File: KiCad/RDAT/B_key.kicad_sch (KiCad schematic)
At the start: 0 parts

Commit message: Connected m.2 E Key
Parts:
- added C25: 22uF/6.3V, symbol Device:C_Small
- added C26: 10uF/6.3v, symbol Device:C_Small
- added C27: 0.1uF/16v, symbol Device:C_Small
- added C28, C29: 0.1uF/16V, symbol Device:C_Small
- added C30: 1uF/6.3v, symbol Device:C_Small
- added C31: 100fP/50V, symbol Device:C_Small
- added D110, D118: SD05_SOD323, Diode_SMD:D_SOD-323, symbol Diode:SD05_SOD323
- added D119, D120, D121, D122: ESD9B5.0ST5G, Diode_SMD:D_SOD-923, symbol Diode:ESD9B5.0ST5G
- added J3: Bus_M.2_Socket_B, symbol Connector:Bus_M.2_Socket_B
- added J4: SIM_Card, symbol Connector:SIM_Card
- added R28, R29: 10k, symbol Device:R_Small_US
- added R30, R78, R79, R83, R84: 0R, symbol Device:R_Small_US
- added R80, R81, R82: 15R, symbol Device:R_Small_US
- added TP13, TP14, TP15, TP16: TestPoint, symbol Connector:TestPoint
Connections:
- new net: J3.6 (~{FULL_CARD_POWER_OFF}), R29.2, R30.2, R78.1
- new net: J3.34 (UIM-DATA), R80.2
- new net: J3.68 (SUSCLK), TP16.1
- new net: J3.1 (CONFIG_3), TP14.1
- new net: J3.66 (SIM_DETECT), R79.1
- new net: J3.21 (CONFIG_0), TP15.1
- new net: J3.23 (GPIO_11), TP13.1
- new net: J3.30 (UIM-RESET), R82.2
- new net: J3.32 (UIM-CLK), R81.2
- new net: C29.2, J3.35 (PETn1/USB3.0-Tx-/SSIC-TxN)
- new net: C28.2, J3.37 (PETp1/USB3.0-Tx+/SSIC-TxP)
- new net: J3.67 (~{RESET}), R83.2, R84.2
- new net: J3.8 (~{W_DISABLE1}), R28.2
- new net: C31.2, J4.6 (VPP)
- new net +3V3: C25.1, C26.1, C27.1, J3.2 (3.3V), J3.4 (3.3V), J3.70 (3.3V), J3.72 (3.3V), J3.74 (3.3V), R28.1, R29.1
- new net GND: C25.2, C26.2, C27.2, C30.2, C31.1, D110.1 (A1), D118.1 (A1), D119.1 (A1), D120.1 (A1), D121.1 (A1), D122.1 (A1), J3.11 (GND), J3.27 (GND), J3.3 (GND), J3.33 (GND), J3.39 (GND), J3.45 (GND), J3.5 (GND), J3.51 (GND), J3.57 (GND), J3.71 (GND), J3.73 (GND), J3.75 (CONFIG_2), J4. (CD), J4.5 (GND)
- new net GPP_D0: R78.2
- new net GPP_D1: R83.1
- new net GPP_E0_SATAXPCIE0: R30.1
- new net GPP_F16_GSXCLK: R84.1
- new net HSIO0_RX_N: J3.29 (PERn1/USB3.0-Rx-/SSIC-RxN)
- new net HSIO0_RX_P: J3.31 (PERp1/USB3.0-Rx+/SSIC-RxP)
- new net HSIO0_TX_N: C29.1
- new net HSIO0_TX_P: C28.1
- new net SIM_CLK: D119.2 (A2), J4.3 (CLK), R81.1
- new net SIM_DATA: J4.7 (I/O), R80.1
- new net SIM_DET: D121.2 (A2), J4. (CD), R79.2
- new net SIM_RST: D120.2 (A2), J4.2 (RST), R82.1
- new net USB2_N1: D118.2 (A2), J3.9 (USB_D-)
- new net USB2_P1: D110.2 (A2), J3.7 (USB_D+)
- new net VCC_SIM: C30.1, D122.2 (A2), J3.36 (UIM-PWR), J4.1 (VCC)
- no-connect marks 0 -> 30
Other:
- note added: "1.8v"

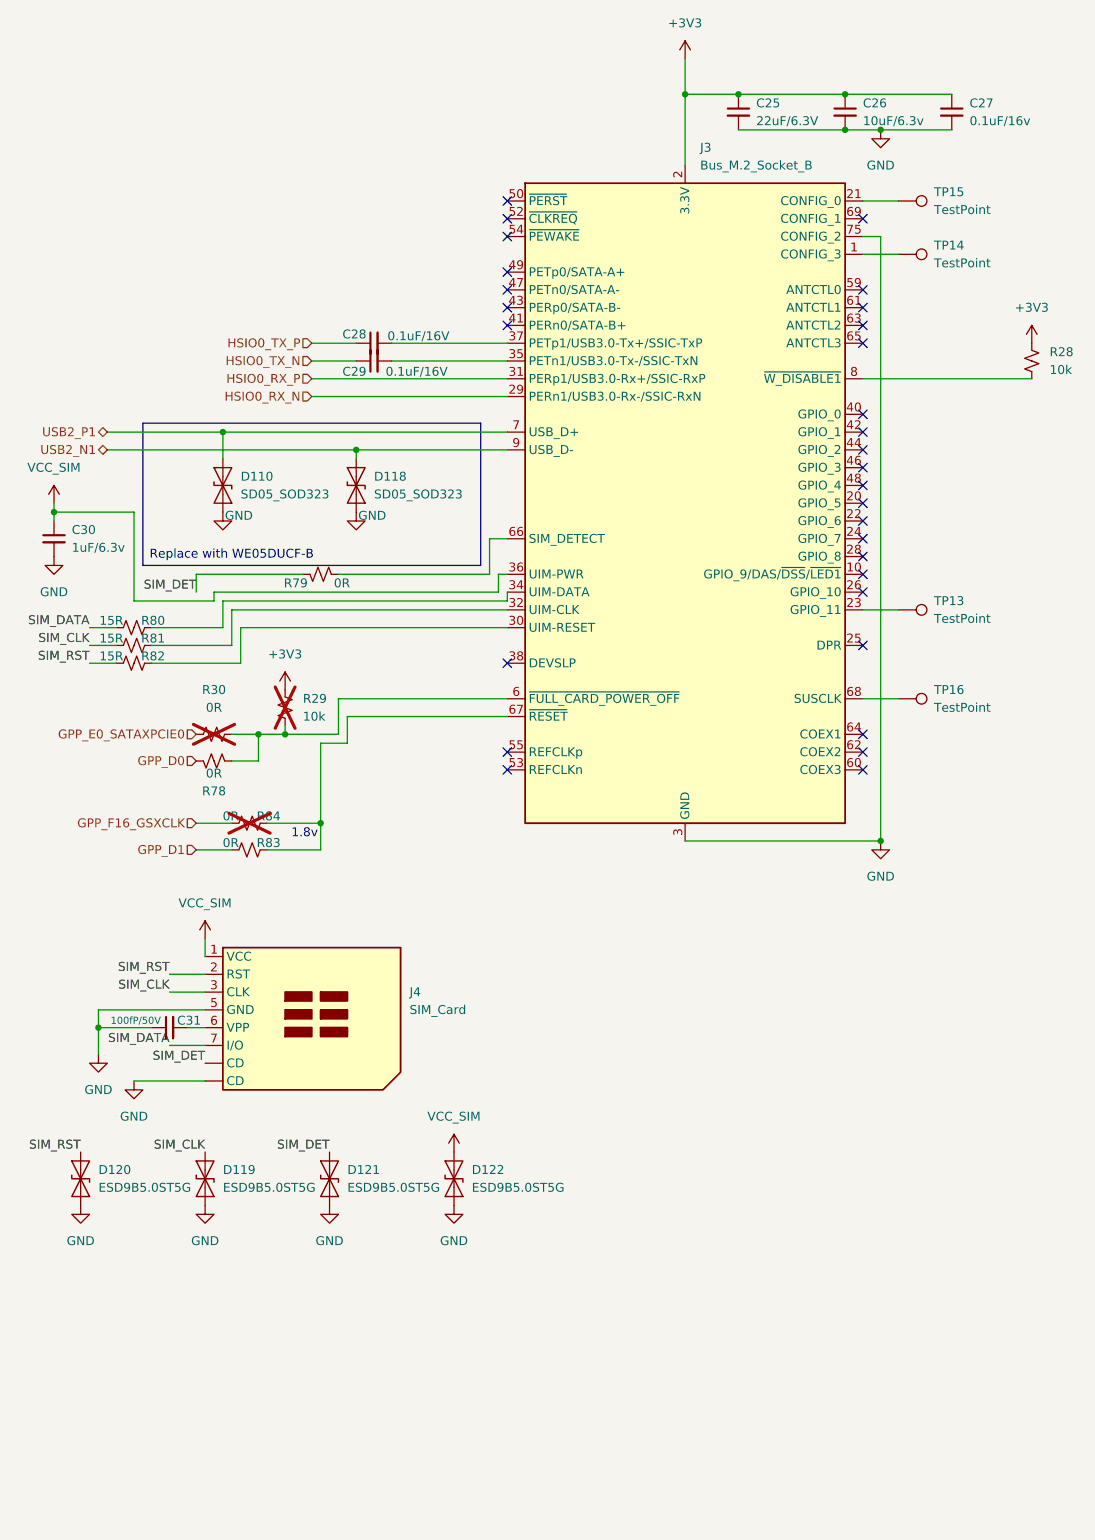
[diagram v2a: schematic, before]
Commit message: Added HDMI connection and marked section for review in schematics; updated column widths in PRL file; added new operating values CSV files for power calculations.
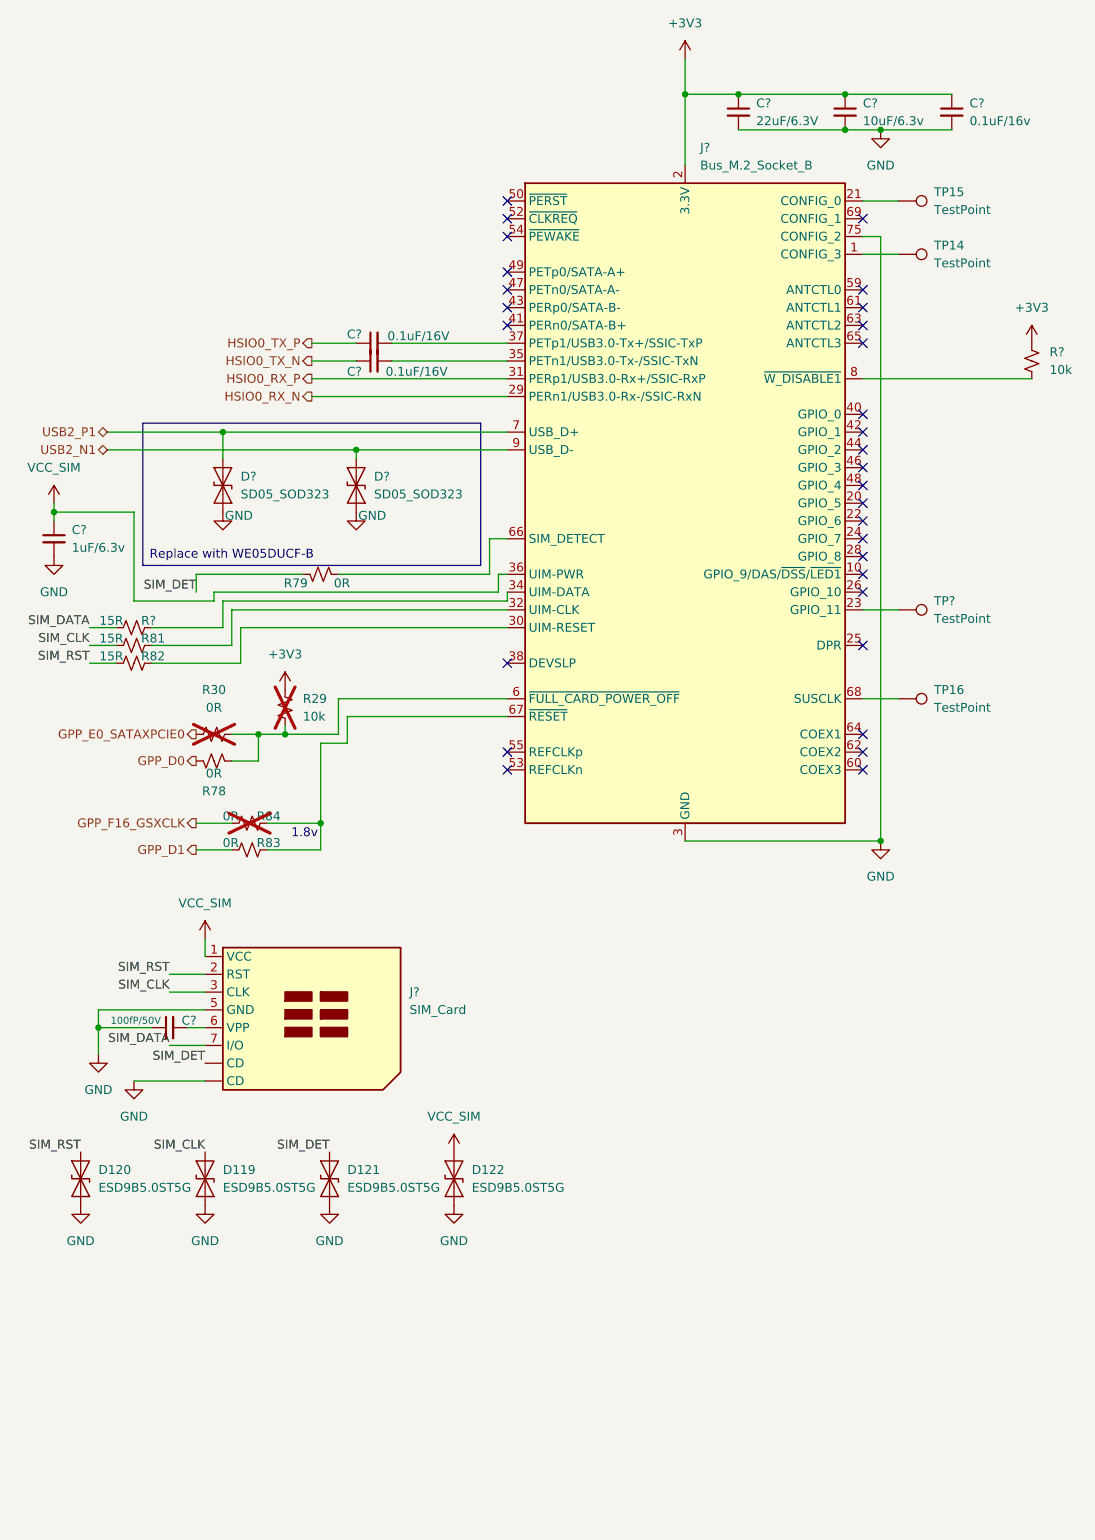
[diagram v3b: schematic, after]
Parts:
- renumbered C25 to C?, C26 to C?, C30 to C?, C27 to C?, C29 to C?, C28 to C?, C31 to C?, D118 to D?, D110 to D?, J3 to J?, J4 to J?, R80 to R?, R28 to R?, TP13 to TP?
